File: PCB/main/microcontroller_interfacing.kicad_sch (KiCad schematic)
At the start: 14 parts, among them IC5 CP2102-GMR, U3 CAT24C256, U4 MICROXNJ

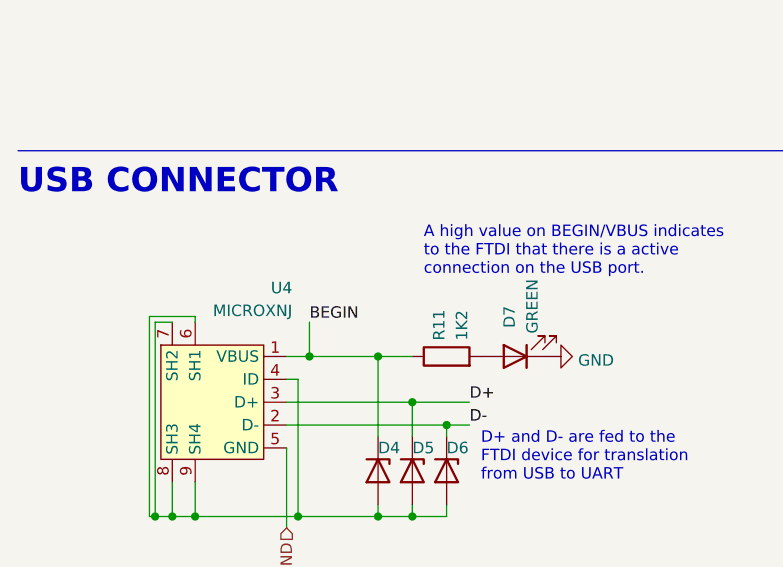
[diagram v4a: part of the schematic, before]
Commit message: Connected voltage supply from USB to power subsystem
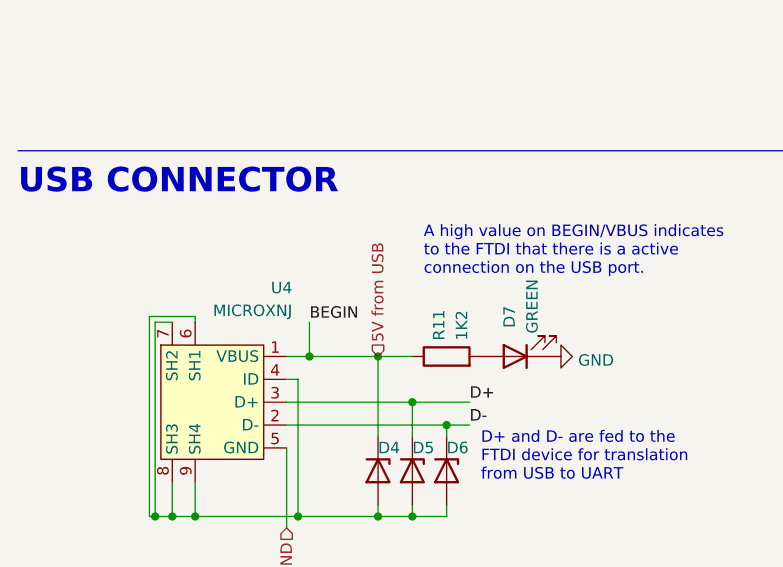
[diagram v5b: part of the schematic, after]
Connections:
- net BEGIN renamed 5V from USB
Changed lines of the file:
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@@
+    (effects (font (size 1.27 1.27)) (justify left))
+  )
+  (hierarchical_label "5V from USB" (shape input) (at 52.705 101.6 90)
     (effects (font (size 1.27 1.27)) (justify left))
   )
